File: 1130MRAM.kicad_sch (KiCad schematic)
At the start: 152 parts, among them IC1 BSV52LT1G, IC10 BSV52LT1G, IC11 BSV52LT1G, IC12 BSV52LT1G, IC13 BSV52LT1G, IC14 BSV52LT1G, IC15 BSV52LT1G, IC16 BSV52LT1G, IC17 BSV52LT1G, IC18 BSV52LT1G, IC2 BSV52LT1G, IC3 BSV52LT1G, IC4 BSV52LT1G, IC5 BSV52LT1G, IC6 BSV52LT1G, IC7 BSV52LT1G, IC8 BSV52LT1G, IC9 BSV52LT1G, J1 Conn_01x09_MountingPin, J1A09 SLTpad, J1A11 SLTpad, J2 Conn_01x09_MountingPin, J3 Conn_01x09_MountingPin, J4 Conn_01x09_MountingPin, J5 Screw_Terminal_01x03, K1E09 SLTpad, K1E11 SLTpad, M1A09 SLTpad, M1A11 SLTpad, M1C09 SLTpad, M1D09 SLTpad, M1E09 SLTpad, M1E11 SLTpad, SW1 SLTpad, U1 MR0A16AYS35, U10 74LVC08A, U11 74LVC08A, U14 74HC00, U15 74HC86, U16 74HC86, U17 74HC86, U18 74HC86, U2 SN74LV240APWR, U3 SN74LV240APWR, U4 LDL1117, U5 LDL1117, U6 74LVC1G14, U7 74LVC08A, U8 74LVC08A, U9 74LVC08A

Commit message: Change base resistors
minot component cahnge
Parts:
- R11, R14, R15, R16, R17, R18, R19, R20, R21, R22, R23, R24, R3, R4, R5, R6: value 2k -> 470
- R12, R13: value 2K -> 470
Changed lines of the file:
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@@
       (effects (font (size 1.27 1.27)) (justify right))
     )
-    (property "Value" "2k" (at 153.67 236.22 0)
+    (property "Value" "470" (at 153.67 236.22 0)
       (effects (font (size 1.27 1.27)) (justify right))
     )
@@
       (effects (font (size 1.27 1.27)))
     )
-    (property "Value" "2k" (at 232.41 196.85 90)
+    (property "Value" "470" (at 232.41 196.85 90)
       (effects (font (size 1.27 1.27)))
     )
@@
       (effects (font (size 1.27 1.27)))
     )
-    (property "Value" "2k" (at 334.01 154.94 90)
+    (property "Value" "470" (at 334.01 154.94 90)
       (effects (font (size 1.27 1.27)))
     )
@@
       (effects (font (size 1.27 1.27)))
     )
-    (property "Value" "2k" (at 193.04 138.43 90)
+    (property "Value" "470" (at 193.04 138.43 90)
       (effects (font (size 1.27 1.27)))
     )
@@
       (effects (font (size 1.27 1.27)) (justify right))
     )
-    (property "Value" "2k" (at 199.39 205.74 0)
+    (property "Value" "470" (at 199.39 205.74 0)
       (effects (font (size 1.27 1.27)) (justify right))
     )
@@
       (effects (font (size 1.27 1.27)) (justify right))
     )
-    (property "Value" "2k" (at 121.92 236.22 0)
+    (property "Value" "470" (at 121.92 236.22 0)
       (effects (font (size 1.27 1.27)) (justify right))
     )
@@
       (effects (font (size 1.27 1.27)) (justify right))
     )
-    (property "Value" "2k" (at 135.89 236.22 0)
+    (property "Value" "470" (at 135.89 236.22 0)
       (effects (font (size 1.27 1.27)) (justify right))
     )
@@
       (effects (font (size 1.27 1.27)) (justify right))
     )
-    (property "Value" "2k" (at 106.68 236.22 0)
+    (property "Value" "470" (at 106.68 236.22 0)
       (effects (font (size 1.27 1.27)) (justify right))
     )
@@
       (effects (font (size 1.27 1.27)))
     )
-    (property "Value" "2k" (at 281.94 123.19 90)
+    (property "Value" "470" (at 281.94 123.19 90)
       (effects (font (size 1.27 1.27)))
     )
@@
       (effects (font (size 1.27 1.27)))
     )
-    (property "Value" "2k" (at 220.98 139.7 90)
+    (property "Value" "470" (at 220.98 139.7 90)
       (effects (font (size 1.27 1.27)))
     )
@@
       (effects (font (size 1.27 1.27)))
     )
-    (property "Value" "2k" (at 247.65 138.43 90)
+    (property "Value" "470" (at 247.65 138.43 90)
       (effects (font (size 1.27 1.27)))
     )
@@
       (effects (font (size 1.27 1.27)))
     )
-    (property "Value" "2K" (at 223.52 175.26 90)
+    (property "Value" "470" (at 223.52 175.26 90)
       (effects (font (size 1.27 1.27)))
     )
@@
       (effects (font (size 1.27 1.27)))
     )
-    (property "Value" "2k" (at 280.67 173.99 90)
+    (property "Value" "470" (at 280.67 173.99 90)
       (effects (font (size 1.27 1.27)))
     )
@@
       (effects (font (size 1.27 1.27)))
     )
-    (property "Value" "2k" (at 173.99 138.43 90)
+    (property "Value" "470" (at 173.99 138.43 90)
       (effects (font (size 1.27 1.27)))
     )
@@
       (effects (font (size 1.27 1.27)))
     )
-    (property "Value" "2k" (at 212.09 198.12 90)
+    (property "Value" "470" (at 212.09 198.12 90)
       (effects (font (size 1.27 1.27)))
     )
@@
       (effects (font (size 1.27 1.27)))
     )
-    (property "Value" "2k" (at 316.23 124.46 90)
+    (property "Value" "470" (at 316.23 124.46 90)
       (effects (font (size 1.27 1.27)))
     )
@@
       (effects (font (size 1.27 1.27)) (justify right))
     )
-    (property "Value" "2K" (at 190.5 199.39 0)
+    (property "Value" "470" (at 190.5 199.39 0)
       (effects (font (size 1.27 1.27)) (justify right))
     )
@@
       (effects (font (size 1.27 1.27)))
     )
-    (property "Value" "2k" (at 334.01 165.1 90)
+    (property "Value" "470" (at 334.01 165.1 90)
       (effects (font (size 1.27 1.27)))
     )

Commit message: Final version of the board and bill of material
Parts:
- added J6: Screw_Terminal_01x01, TerminalBlock_WAGO:TerminalBlock_WAGO_236-101_1x01_P5.00mm_45Degree, symbol Connector:Screw_Terminal_01x01
- J5: footprint Connector_Phoenix_MC_HighVoltage:PhoenixContact_MCV_1,5_2-G-5.08_1x02_P5.08mm_Vertical -> TerminalBlock_WAGO:TerminalBlock_WAGO_236-102_1x02_P5.00mm_45Degree
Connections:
- net GND: now also J6.1 (Pin_1)
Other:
- note added: "braided ground"
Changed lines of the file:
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@@
   (junction (at 143.51 55.88) (diameter 0) (color 0 0 0 0)
   )
+  (junction (at 50.8 63.5) (diameter 0) (color 0 0 0 0)
+  )
   (junction (at 146.05 256.54) (diameter 0) (color 0 0 0 0)
   )
@@
     (stroke (width 0) (type default))
   )
-  (wire (pts (xy 44.45 63.5) (xy 73.66 63.5))
+  (wire (pts (xy 44.45 63.5) (xy 50.8 63.5))
     (stroke (width 0) (type default))
   )
@@
     (stroke (width 0) (type default))
   )
+  (wire (pts (xy 50.8 58.42) (xy 50.8 63.5))
+    (stroke (width 0) (type default))
+  )
   (wire (pts (xy 146.05 208.28) (xy 85.09 208.28))
     (stroke (width 0) (type default))
@@
     (stroke (width 0) (type default))
   )
+  (wire (pts (xy 50.8 63.5) (xy 73.66 63.5))
+    (stroke (width 0) (type default))
+  )
   (wire (pts (xy 186.69 25.4) (xy 186.69 15.24))
     (stroke (width 0) (type default))
@@
     (effects (font (size 1.27 1.27)) (justify left bottom))
   )
+  (text "braided ground" (at 49.53 55.88 0)
+    (effects (font (size 1.27 1.27)) (justify left bottom))
+  )
   (text "CMOD S7 upper left connector" (at 17.78 213.36 0)
     (effects (font (size 1.27 1.27)) (justify left bottom))
@@
     )
   )
+  (symbol (lib_id "Connector:Screw_Terminal_01x01") (at 55.88 58.42 0) (unit 1)
+    (in_bom yes) (on_board yes) (dnp no) (fields_autoplaced)
+    (property "Reference" "J6" (at 58.42 57.15 0)
+      (effects (font (size 1.27 1.27)) (justify left))
+    )
+    (property "Value" "Screw_Terminal_01x01" (at 58.42 59.69 0)
+      (effects (font (size 1.27 1.27)) (justify left) hide)
+    )
+    (property "Footprint" "TerminalBlock_WAGO:TerminalBlock_WAGO_236-101_1x01_P5.00mm_45Degree" (at 55.88 58.42 0)
+      (effects (font (size 1.27 1.27)) hide)
+    )
+    (property "Datasheet" "~" (at 55.88 58.42 0)
+      (effects (font (size 1.27 1.27)) hide)
+    )
+    (pin "1")
+    (instances
+      (project "1130MRAM"
+        (path "/45ef7c51-4ae3-4e46-9e96-bfd8868dc953"
+          (reference "J6") (unit 1)
+        )
+      )
+    )
+  )
   (symbol (lib_id "1130mram:74HC86") (at 335.28 250.19 0) (unit 5)
     (in_bom yes) (on_board yes) (dnp no) (fields_autoplaced)
@@
       (effects (font (size 1.27 1.27)) (justify left) hide)
     )
-    (property "Footprint" "Connector_Phoenix_MC_HighVoltage:PhoenixContact_MCV_1,5_2-G-5.08_1x02_P5.08mm_Vertical" (at 95.25 60.96 0)
+    (property "Footprint" "TerminalBlock_WAGO:TerminalBlock_WAGO_236-102_1x02_P5.00mm_45Degree" (at 95.25 60.96 0)
       (effects (font (size 1.27 1.27)) hide)
     )

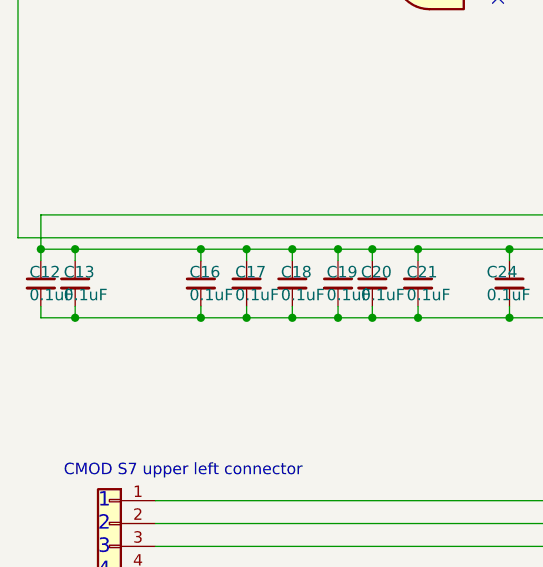
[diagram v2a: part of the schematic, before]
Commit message: Improved PCB design
improved ground paths for MRAM chiip, added 10uF decoupling capacitor next to .1uF capacitor. 

opened solder mask for four ground pads to solder magnetic shield over chip
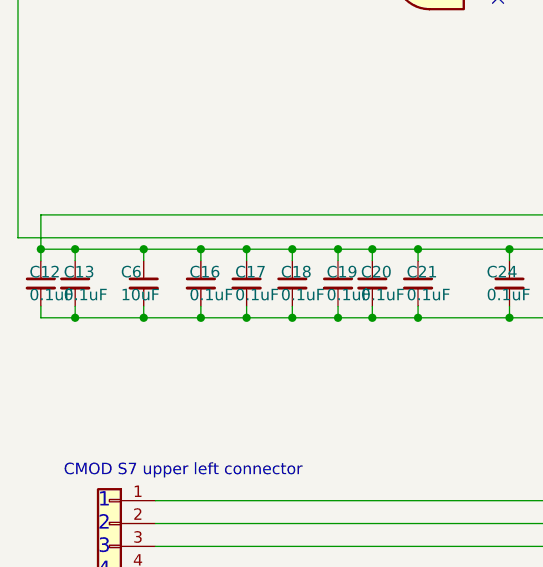
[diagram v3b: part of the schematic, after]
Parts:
- added C6: 10uF, Capacitor_SMD:C_0805_2012Metric, symbol Device:C_Small
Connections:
- net +3.3V: now also C6.1
- net GND: now also C6.2
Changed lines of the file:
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@@
   (junction (at 299.72 72.39) (diameter 0) (color 0 0 0 0)
   )
+  (junction (at 26.67 195.58) (diameter 0) (color 0 0 0 0)
+  )
   (junction (at 335.28 237.49) (diameter 0) (color 0 0 0 0)
   )
@@
   (junction (at 166.37 90.17) (diameter 0) (color 0 0 0 0)
   )
+  (junction (at 26.67 187.96) (diameter 0) (color 0 0 0 0)
+  )
   (junction (at 54.61 30.48) (diameter 0) (color 0 0 0 0)
   )
@@
     (stroke (width 0) (type default))
   )
-  (wire (pts (xy 19.05 187.96) (xy 33.02 187.96))
+  (wire (pts (xy 19.05 187.96) (xy 26.67 187.96))
     (stroke (width 0) (type default))
   )
@@
     (stroke (width 0) (type default))
   )
+  (wire (pts (xy 26.67 195.58) (xy 33.02 195.58))
+    (stroke (width 0) (type default))
+  )
   (wire (pts (xy 82.55 187.96) (xy 76.2 187.96))
     (stroke (width 0) (type default))
@@
     (stroke (width 0) (type default))
   )
+  (wire (pts (xy 26.67 187.96) (xy 26.67 189.23))
+    (stroke (width 0) (type default))
+  )
   (wire (pts (xy 27.94 220.98) (xy 86.36 220.98))
     (stroke (width 0) (type default))
@@
     (stroke (width 0) (type default))
   )
+  (wire (pts (xy 26.67 194.31) (xy 26.67 195.58))
+    (stroke (width 0) (type default))
+  )
   (wire (pts (xy 391.16 133.35) (xy 391.16 13.97))
     (stroke (width 0) (type default))
@@
     (stroke (width 0) (type default))
   )
+  (wire (pts (xy 26.67 187.96) (xy 33.02 187.96))
+    (stroke (width 0) (type default))
+  )
   (wire (pts (xy 167.64 64.77) (xy 167.64 92.71))
     (stroke (width 0) (type default))
@@
     (stroke (width 0) (type default))
   )
-  (wire (pts (xy 19.05 195.58) (xy 33.02 195.58))
+  (wire (pts (xy 19.05 195.58) (xy 26.67 195.58))
     (stroke (width 0) (type default))
   )
@@
         )
       )
+    )
+  )
+  (symbol (lib_id "Device:C_Small") (at 26.67 191.77 0) (unit 1)
+    (in_bom yes) (on_board yes) (dnp no)
+    (property "Reference" "C6" (at 24.13 190.5 0)
+      (effects (font (size 1.27 1.27)) (justify left))
+    )
+    (property "Value" "10uF" (at 24.13 193.04 0)
+      (effects (font (size 1.27 1.27)) (justify left))
+    )
+    (property "Footprint" "Capacitor_SMD:C_0805_2012Metric" (at 26.67 191.77 0)
+      (effects (font (size 1.27 1.27)) hide)
+    )
+    (property "Datasheet" "~" (at 26.67 191.77 0)
+      (effects (font (size 1.27 1.27)) hide)
+    )
+    (pin "1")
+    (pin "2")
+    (instances
+      (project "1130MRAM"
+        (path "/45ef7c51-4ae3-4e46-9e96-bfd8868dc953"
+          (reference "C6") (unit 1)
+        )
+      )
